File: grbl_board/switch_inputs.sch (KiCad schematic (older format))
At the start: 22 parts, among them J10 DOOR, J11 PROBE, J12 INP, J13 LIM, U10 6N137, U11 6N137, U12 6N137, U13 6N137, U14 6N137, U15 6N137, U16 6N137, U17 6N137, U9 6N137

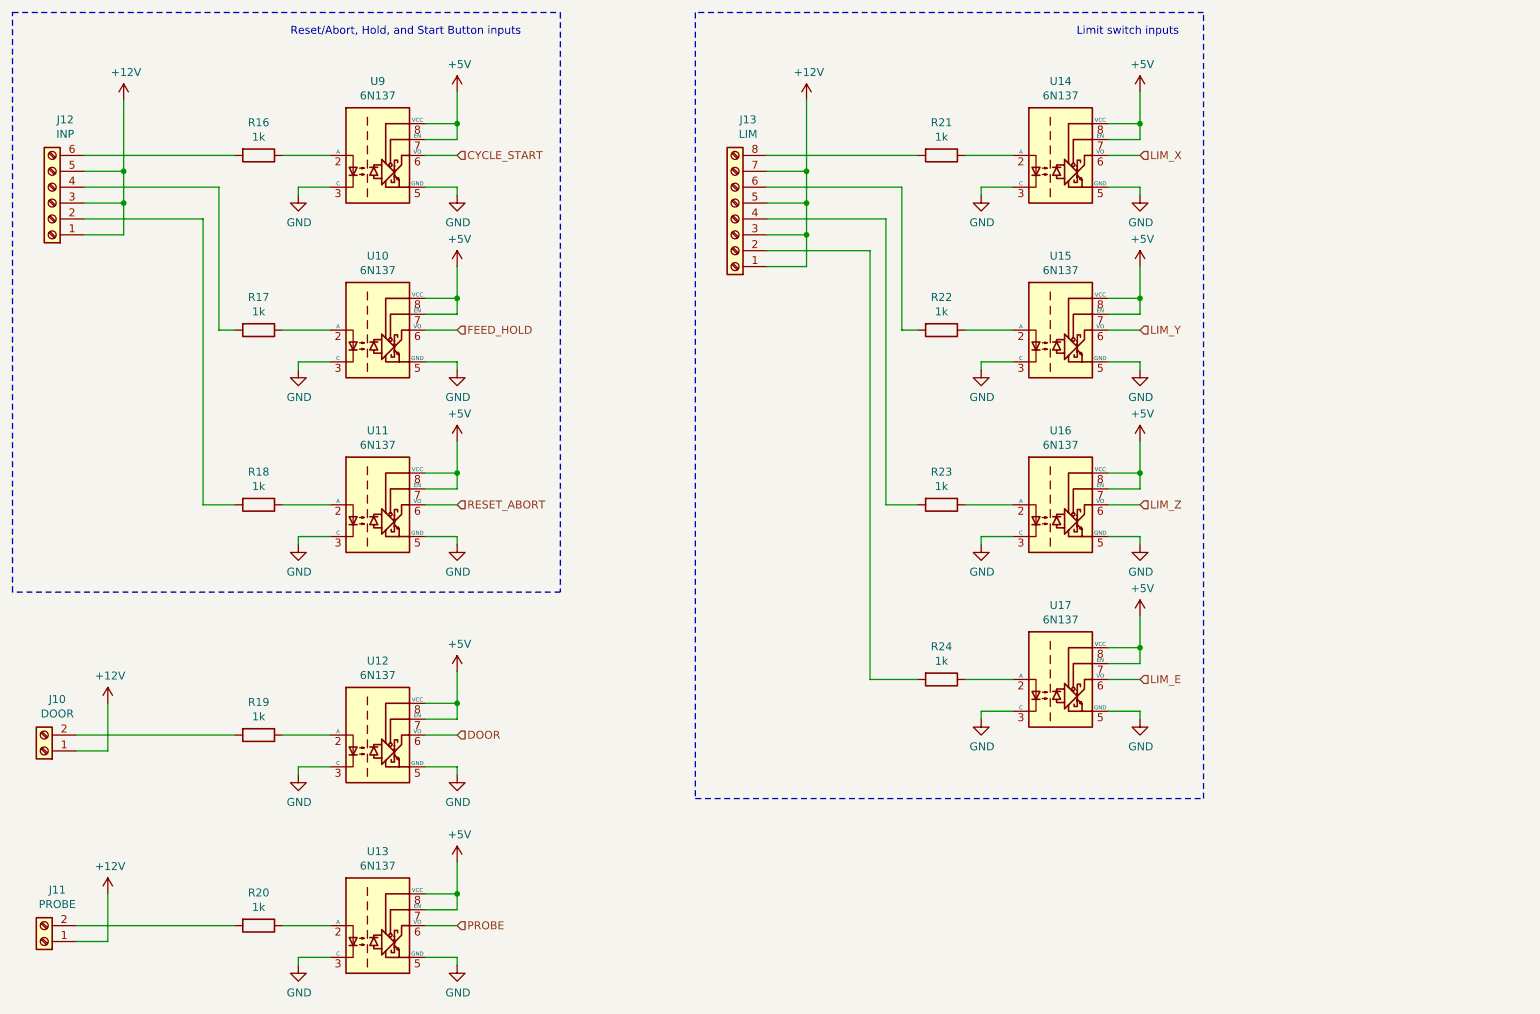
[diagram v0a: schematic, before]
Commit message: fixed pullup resistors on board, and 5v regulator overheating, and stepper driver flipped
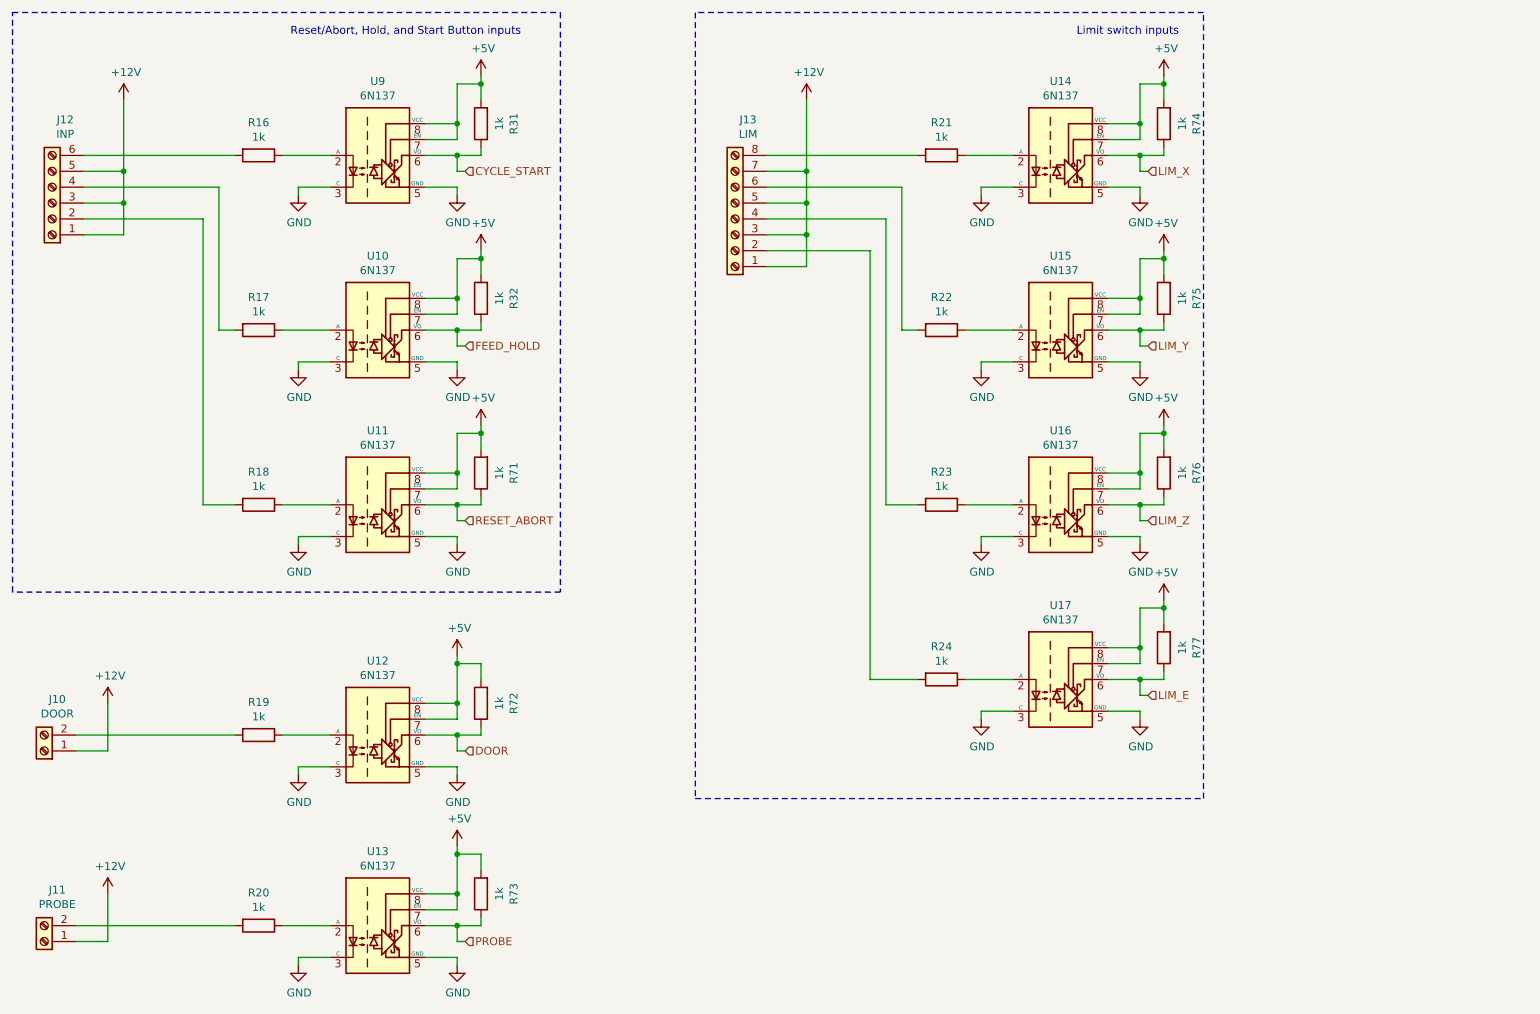
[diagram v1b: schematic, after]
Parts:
- added R31, R32, R71, R72, R73, R74, R75, R76, R77: 1k, Resistor_SMD:R_0805_2012Metric_Pad1.15x1.40mm_HandSolder, symbol Device:R
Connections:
- net +5V: now also R31.2, R32.2, R71.2, R72.2, R73.2, R74.2, R75.2, R76.2, R77.2
- net CYCLE_START: now also R31.1
- net DOOR: now also R72.1
- net FEED_HOLD: now also R32.1
- net LIM_E: now also R77.1
- net LIM_X: now also R74.1
- net LIM_Y: now also R75.1
- net LIM_Z: now also R76.1
- net PROBE: now also R73.1
- net RESET_ABORT: now also R71.1

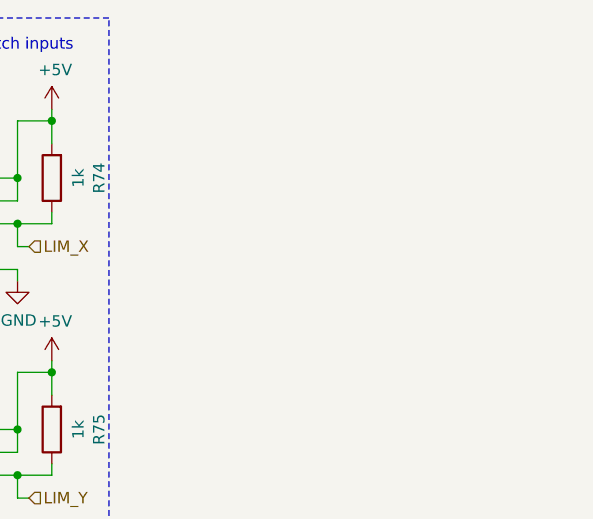
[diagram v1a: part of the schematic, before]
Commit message: added limit switch indicator LEDs
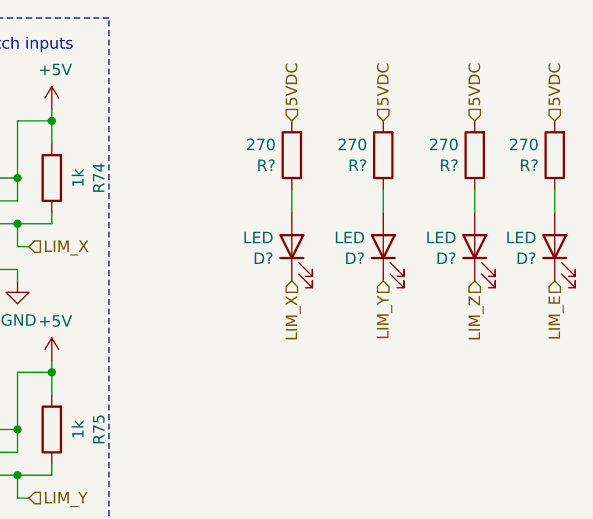
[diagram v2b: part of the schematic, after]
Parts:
- added D? (x4): LED, LED_SMD:LED_1206_3216Metric_Pad1.42x1.75mm_HandSolder, symbol Device:LED
- added R? (x4): 270, Resistor_SMD:R_0805_2012Metric_Pad1.15x1.40mm_HandSolder, symbol Device:R
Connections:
- net LIM_E: now also D?.1 (K)
- net LIM_X: now also D?.1 (K)
- net LIM_Y: now also D?.1 (K)
- net LIM_Z: now also D?.1 (K)
- new net: D?.2 (A), R?.1 (x4)
- new net 5VDC: R?.2, R?.2, R?.2, R?.2
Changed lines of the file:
@@
 Wire Wire Line
 	4050 5800 4000 5800
+Text HLabel 10650 1600 1    50   Input ~ 0
+5VDC
+$Comp
+L Device:LED D?
+U 1 1 61C80669
+P 10650 2150
+AR Path="/61764E0B/61C80669" Ref="D?"  Part="1"
+AR Path="/619755E7/61C80669" Ref="D?"  Part="1"
+AR Path="/61D39570/61C80669" Ref="D?"  Part="1"
+F 0 "D?" V 10597 2230 50  0000 L CNN
+F 1 "LED" V 10688 2230 50  0000 L CNN
+F 2 "LED_SMD:LED_1206_3216Metric_Pad1.42x1.75mm_HandSolder" H 10650 2150 50  0001 C CNN
+F 3 "https://media.digikey.com/pdf/Data%20Sheets/Stanley%20Electric%20PDFs/1101W_Series.pdf" H 10650 2150 50  0001 C CNN
+F 4 "404-1046-1-ND" H 10650 2150 50  0001 C CNN "Digikey Part No."
+	1    10650 2150
+	0    -1   -1   0
+$EndComp
+$Comp
+L Device:R R?
+U 1 1 61C80662
+P 10650 1750
+AR Path="/61764E0B/61C80662" Ref="R?"  Part="1"
+AR Path="/619755E7/61C80662" Ref="R?"  Part="1"
+AR Path="/61D39570/61C80662" Ref="R?"  Part="1"
+F 0 "R?" H 10720 1796 50  0000 L CNN
+F 1 "270" H 10720 1705 50  0000 L CNN
+F 2 "Resistor_SMD:R_0805_2012Metric_Pad1.15x1.40mm_HandSolder" V 10580 1750 50  0001 C CNN
+F 3 "https://www.yageo.com/upload/media/product/productsearch/datasheet/rchip/PYu-SR_20105_RoHS_L_9.pdf" H 10650 1750 50  0001 C CNN
+F 4 "YAG6172CT-ND" H 10650 1750 50  0001 C CNN "Digikey Part No."
+	1    10650 1750
+	-1   0    0    1
+$EndComp
+Wire Wire Line
+	10650 1900 10650 2000
+Text HLabel 10300 1600 1    50   Input ~ 0
+5VDC
+$Comp
+L Device:LED D?
+U 1 1 61C6CA4A
+P 10300 2150
+AR Path="/61764E0B/61C6CA4A" Ref="D?"  Part="1"
+AR Path="/619755E7/61C6CA4A" Ref="D?"  Part="1"
+AR Path="/61D39570/61C6CA4A" Ref="D?"  Part="1"
+F 0 "D?" V 10247 2230 50  0000 L CNN
+F 1 "LED" V 10338 2230 50  0000 L CNN
+F 2 "LED_SMD:LED_1206_3216Metric_Pad1.42x1.75mm_HandSolder" H 10300 2150 50  0001 C CNN
+F 3 "https://media.digikey.com/pdf/Data%20Sheets/Stanley%20Electric%20PDFs/1101W_Series.pdf" H 10300 2150 50  0001 C CNN
+F 4 "404-1046-1-ND" H 10300 2150 50  0001 C CNN "Digikey Part No."
+	1    10300 2150
+	0    -1   -1   0
+$EndComp
+$Comp
+L Device:R R?
+U 1 1 61C6CA43
+P 10300 1750
+AR Path="/61764E0B/61C6CA43" Ref="R?"  Part="1"
+AR Path="/619755E7/61C6CA43" Ref="R?"  Part="1"
+AR Path="/61D39570/61C6CA43" Ref="R?"  Part="1"
+F 0 "R?" H 10370 1796 50  0000 L CNN
+F 1 "270" H 10370 1705 50  0000 L CNN
+F 2 "Resistor_SMD:R_0805_2012Metric_Pad1.15x1.40mm_HandSolder" V 10230 1750 50  0001 C CNN
+F 3 "https://www.yageo.com/upload/media/product/productsearch/datasheet/rchip/PYu-SR_20105_RoHS_L_9.pdf" H 10300 1750 50  0001 C CNN
+F 4 "YAG6172CT-ND" H 10300 1750 50  0001 C CNN "Digikey Part No."
+	1    10300 1750
+	-1   0    0    1
+$EndComp
+Wire Wire Line
+	10300 1900 10300 2000
+Text HLabel 9900 1600 1    50   Input ~ 0
+5VDC
+$Comp
+L Device:LED D?
+U 1 1 61C6334D
+P 9900 2150
+AR Path="/61764E0B/61C6334D" Ref="D?"  Part="1"
+AR Path="/619755E7/61C6334D" Ref="D?"  Part="1"
+AR Path="/61D39570/61C6334D" Ref="D?"  Part="1"
+F 0 "D?" V 9847 2230 50  0000 L CNN
+F 1 "LED" V 9938 2230 50  0000 L CNN
+F 2 "LED_SMD:LED_1206_3216Metric_Pad1.42x1.75mm_HandSolder" H 9900 2150 50  0001 C CNN
+F 3 "https://media.digikey.com/pdf/Data%20Sheets/Stanley%20Electric%20PDFs/1101W_Series.pdf" H 9900 2150 50  0001 C CNN
+F 4 "404-1046-1-ND" H 9900 2150 50  0001 C CNN "Digikey Part No."
+	1    9900 2150
+	0    -1   -1   0
+$EndComp
+$Comp
+L Device:R R?
+U 1 1 61C63346
+P 9900 1750
+AR Path="/61764E0B/61C63346" Ref="R?"  Part="1"
+AR Path="/619755E7/61C63346" Ref="R?"  Part="1"
+AR Path="/61D39570/61C63346" Ref="R?"  Part="1"
+F 0 "R?" H 9970 1796 50  0000 L CNN
+F 1 "270" H 9970 1705 50  0000 L CNN
+F 2 "Resistor_SMD:R_0805_2012Metric_Pad1.15x1.40mm_HandSolder" V 9830 1750 50  0001 C CNN
+F 3 "https://www.yageo.com/upload/media/product/productsearch/datasheet/rchip/PYu-SR_20105_RoHS_L_9.pdf" H 9900 1750 50  0001 C CNN
+F 4 "YAG6172CT-ND" H 9900 1750 50  0001 C CNN "Digikey Part No."
+	1    9900 1750
+	-1   0    0    1
+$EndComp
+Wire Wire Line
+	9900 1900 9900 2000
+Wire Wire Line
+	9500 1900 9500 2000
+$Comp
+L Device:R R?
+U 1 1 61C59CE7
+P 9500 1750
+AR Path="/61764E0B/61C59CE7" Ref="R?"  Part="1"
+AR Path="/619755E7/61C59CE7" Ref="R?"  Part="1"
+AR Path="/61D39570/61C59CE7" Ref="R?"  Part="1"
+F 0 "R?" H 9570 1796 50  0000 L CNN
+F 1 "270" H 9570 1705 50  0000 L CNN
+F 2 "Resistor_SMD:R_0805_2012Metric_Pad1.15x1.40mm_HandSolder" V 9430 1750 50  0001 C CNN
+F 3 "https://www.yageo.com/upload/media/product/productsearch/datasheet/rchip/PYu-SR_20105_RoHS_L_9.pdf" H 9500 1750 50  0001 C CNN
+F 4 "YAG6172CT-ND" H 9500 1750 50  0001 C CNN "Digikey Part No."
+	1    9500 1750
+	-1   0    0    1
+$EndComp
+$Comp
+L Device:LED D?
+U 1 1 61C59CEE
+P 9500 2150
+AR Path="/61764E0B/61C59CEE" Ref="D?"  Part="1"
+AR Path="/619755E7/61C59CEE" Ref="D?"  Part="1"
+AR Path="/61D39570/61C59CEE" Ref="D?"  Part="1"
+F 0 "D?" V 9447 2230 50  0000 L CNN
+F 1 "LED" V 9538 2230 50  0000 L CNN
+F 2 "LED_SMD:LED_1206_3216Metric_Pad1.42x1.75mm_HandSolder" H 9500 2150 50  0001 C CNN
+F 3 "https://media.digikey.com/pdf/Data%20Sheets/Stanley%20Electric%20PDFs/1101W_Series.pdf" H 9500 2150 50  0001 C CNN
+F 4 "404-1046-1-ND" H 9500 2150 50  0001 C CNN "Digikey Part No."
+	1    9500 2150
+	0    -1   -1   0
+$EndComp
+Text HLabel 9500 1600 1    50   Input ~ 0
+5VDC
+Text HLabel 9500 2300 3    50   Input ~ 0
+LIM_X
+Text HLabel 9900 2300 3    50   Input ~ 0
+LIM_Y
+Text HLabel 10300 2300 3    50   Input ~ 0
+LIM_Z
+Text HLabel 10650 2300 3    50   Input ~ 0
+LIM_E
 $EndSCHEMATC

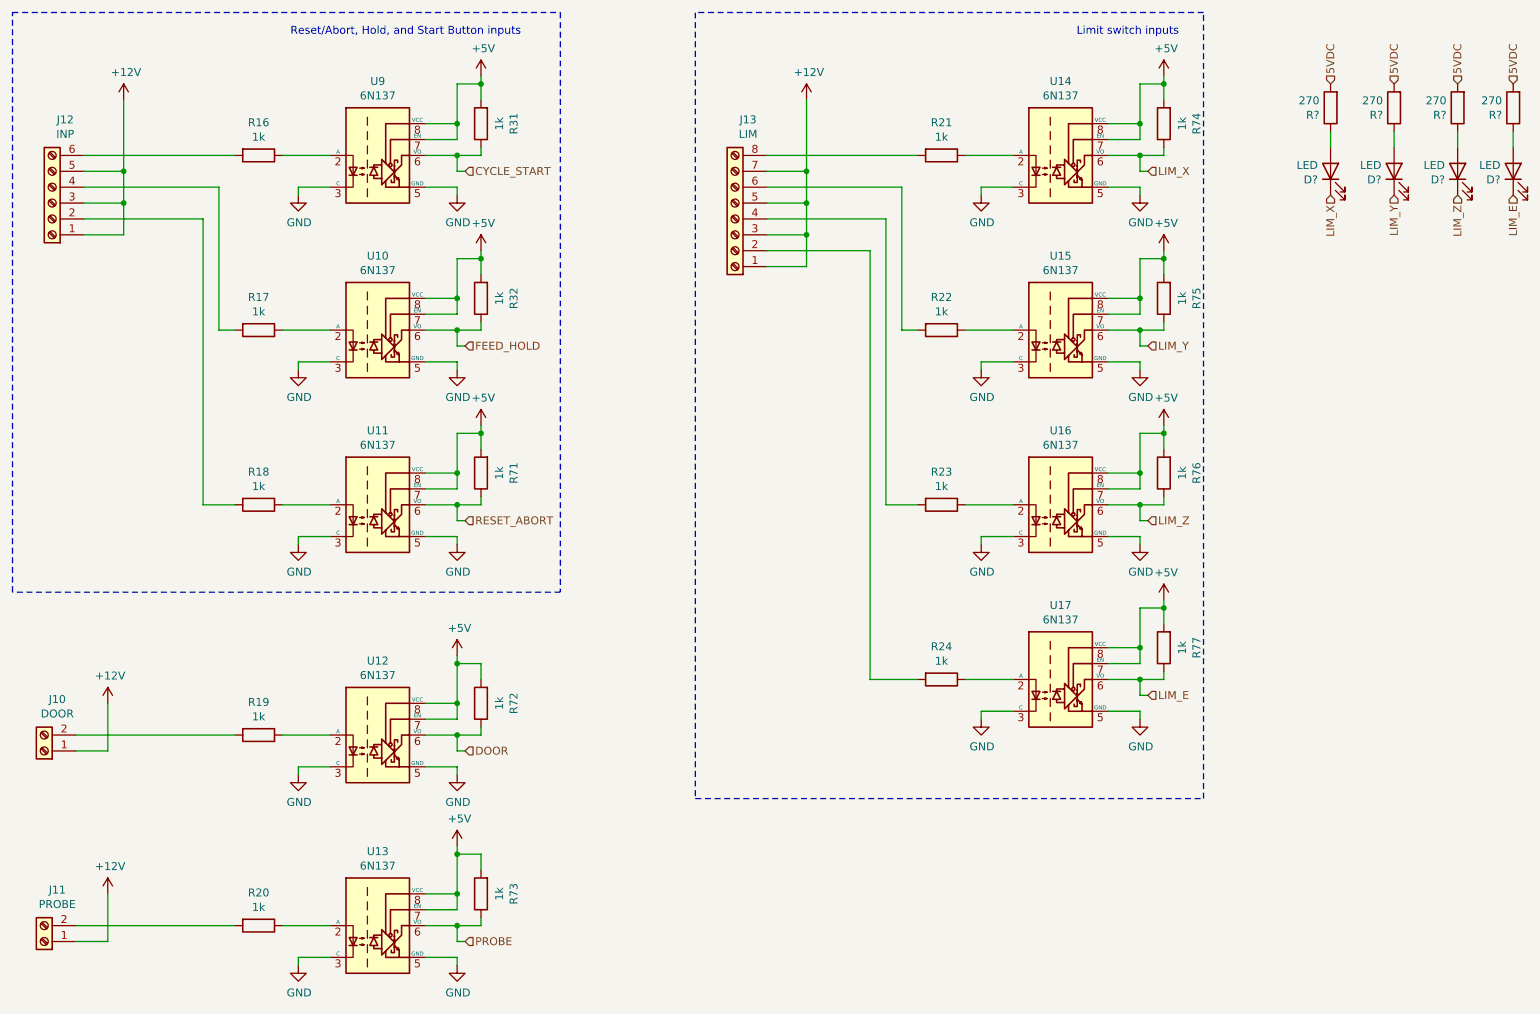
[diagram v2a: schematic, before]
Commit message: updated board with 24V reg
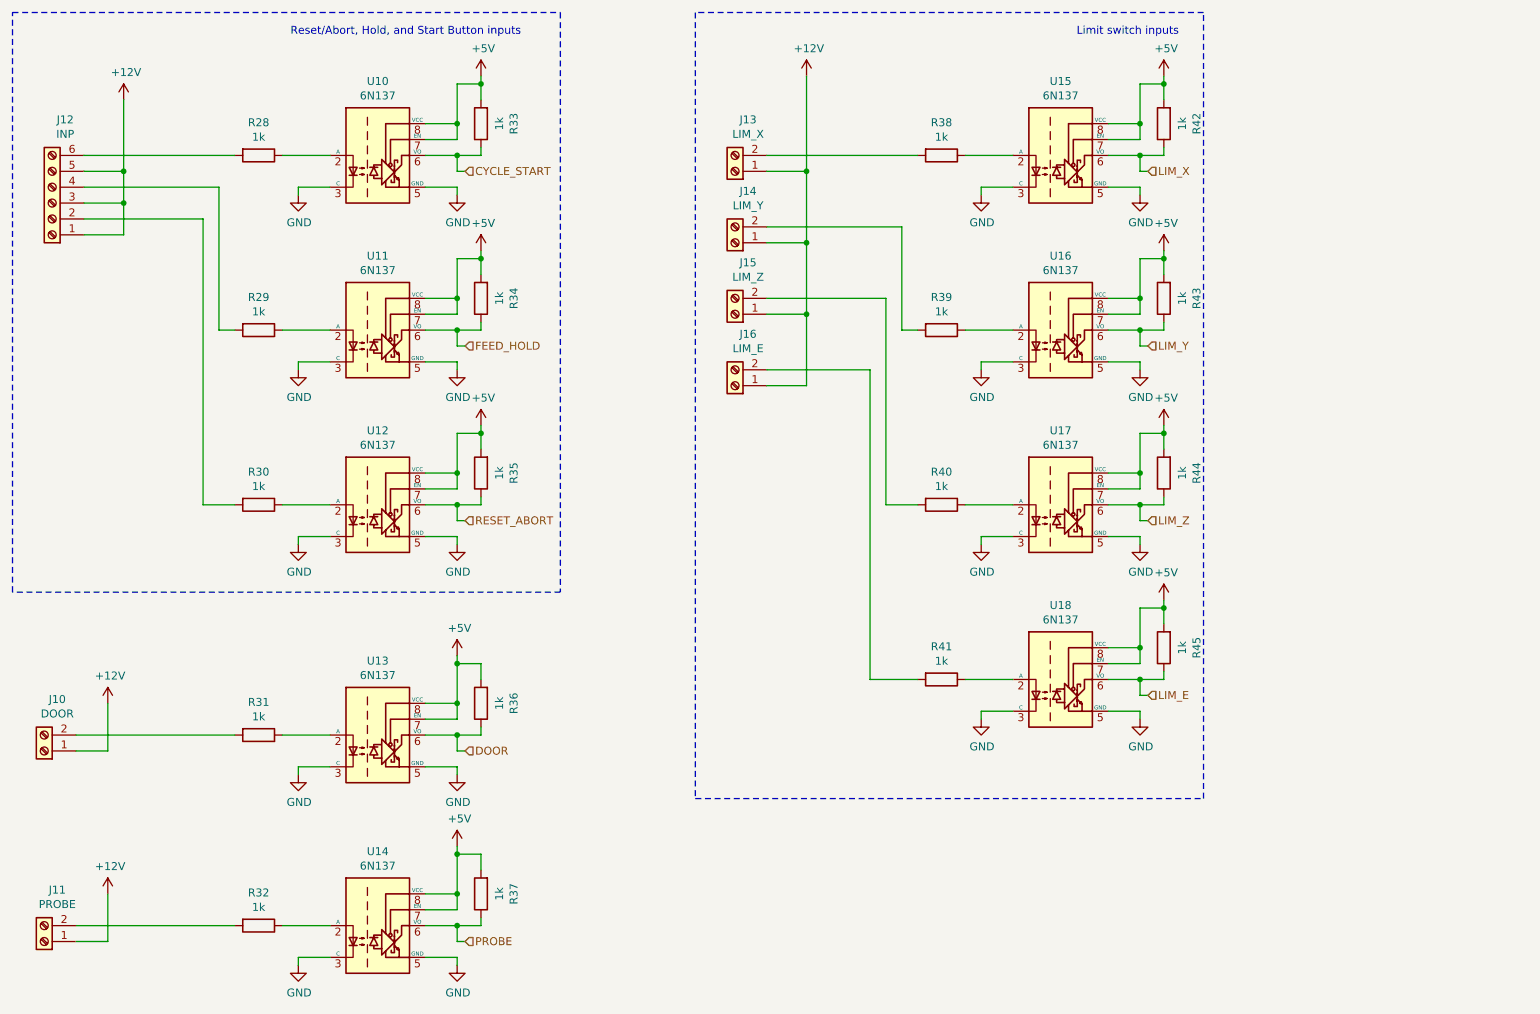
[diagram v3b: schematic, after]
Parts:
- removed D? (x4): LED, LED_SMD:LED_1206_3216Metric_Pad1.42x1.75mm_HandSolder, symbol Device:LED
- removed J13: LIM, Connector_Phoenix_MC:PhoenixContact_MC_1,5_8-G-3.81_1x08_P3.81mm_Horizontal, symbol Connector:Screw_Terminal_01x08
- removed R? (x4): 270, Resistor_SMD:R_0805_2012Metric_Pad1.15x1.40mm_HandSolder, symbol Device:R
- added J13: LIM_X, Connector_Phoenix_MC:PhoenixContact_MC_1,5_2-G-3.81_1x02_P3.81mm_Horizontal, symbol Connector:Screw_Terminal_01x02
- added J14: LIM_Y, Connector_Phoenix_MC:PhoenixContact_MC_1,5_2-G-3.81_1x02_P3.81mm_Horizontal, symbol Connector:Screw_Terminal_01x02
- added J15: LIM_Z, Connector_Phoenix_MC:PhoenixContact_MC_1,5_2-G-3.81_1x02_P3.81mm_Horizontal, symbol Connector:Screw_Terminal_01x02
- added J16: LIM_E, Connector_Phoenix_MC:PhoenixContact_MC_1,5_2-G-3.81_1x02_P3.81mm_Horizontal, symbol Connector:Screw_Terminal_01x02
- renumbered R16 to R28, R17 to R29, R18 to R30, R19 to R31, R20 to R32, R31 to R33, R32 to R34, R71 to R35, R72 to R36, R73 to R37, R21 to R38, R22 to R39, R23 to R40, R24 to R41, R74 to R42, R75 to R43, R76 to R44, R77 to R45, U9 to U10, U10 to U11, U11 to U12, U12 to U13, U13 to U14, U14 to U15, U15 to U16, U16 to U17, U17 to U18
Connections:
- net +12V: now also J13.1 (Pin_1), J14.1 (Pin_1), J15.1 (Pin_1), J16.1 (Pin_1)
- net at R38.2: now also J13.2 (Pin_2)
- net at R39.2: now also J14.2 (Pin_2)
- net at R40.2: now also J15.2 (Pin_2)
- net at R41.2: now also J16.2 (Pin_2)
